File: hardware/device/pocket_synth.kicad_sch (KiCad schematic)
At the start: 0 parts

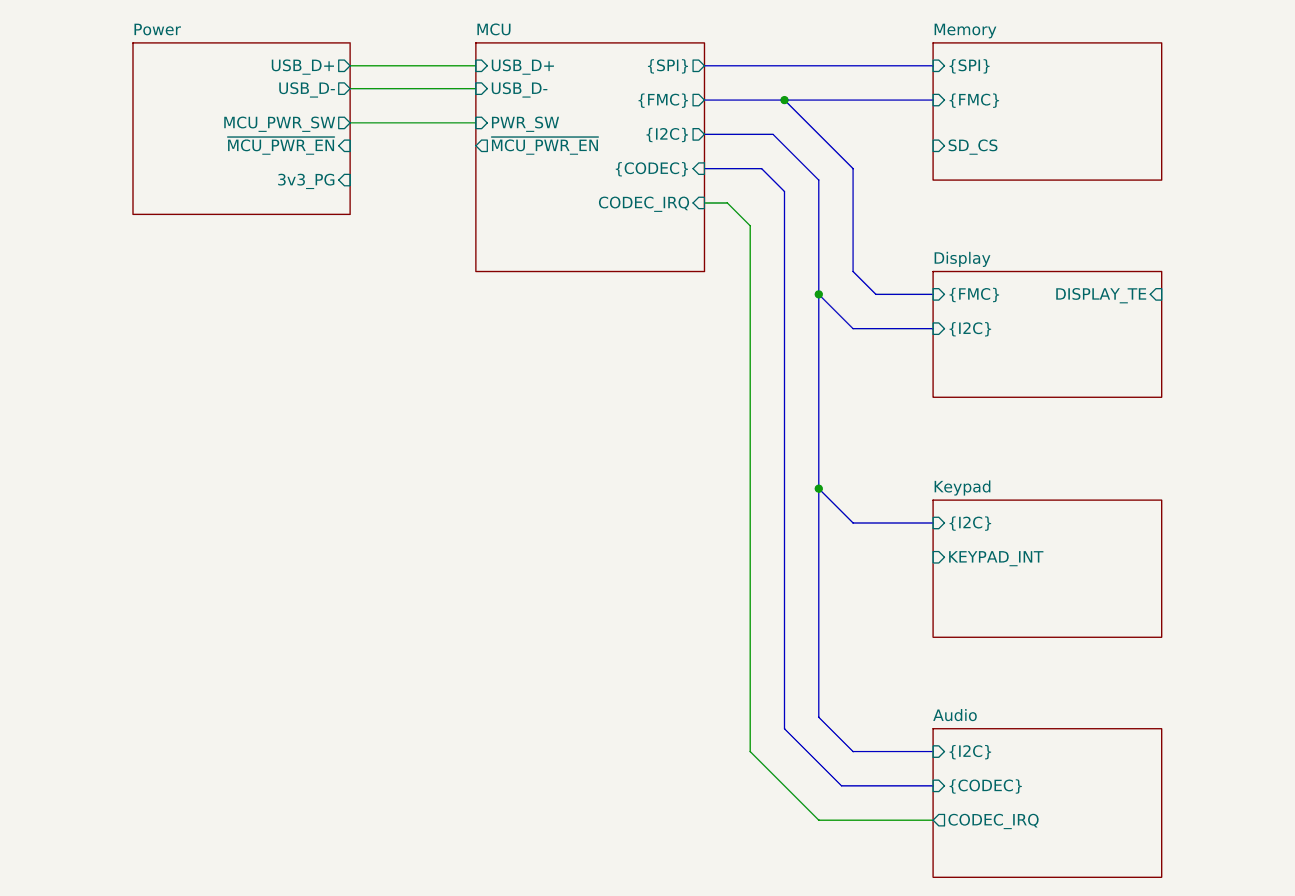
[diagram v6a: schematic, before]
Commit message: chore: audio routing and UART port mapping
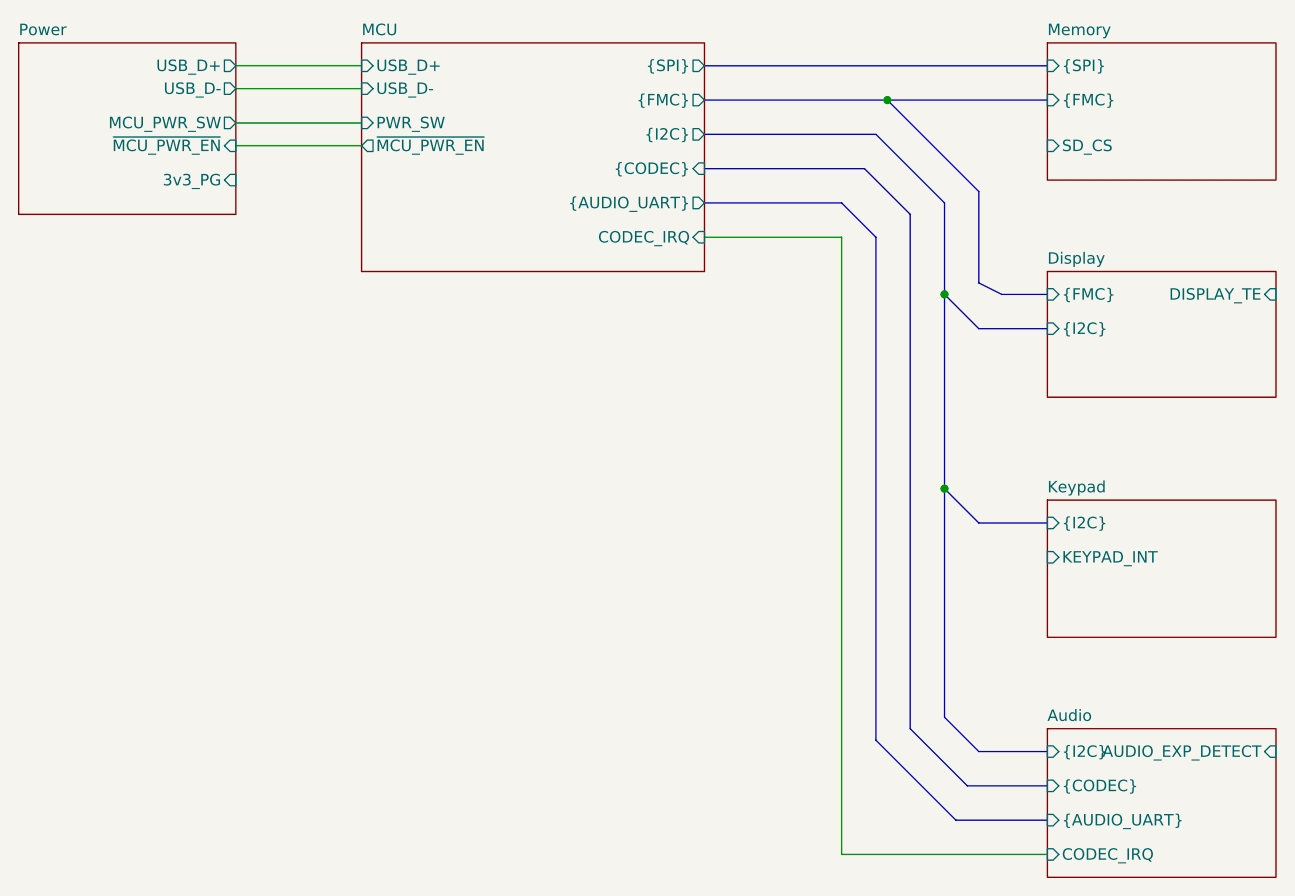
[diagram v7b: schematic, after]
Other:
- sheet Audio ports: added AUDIO_EXP_DETECT, {AUDIO_UART}; removed none
- sheet MCU ports: added {AUDIO_UART}; removed none
